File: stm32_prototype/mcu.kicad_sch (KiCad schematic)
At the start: 26 parts, among them SW1 BOOT0, SW2 RESET, U1 STM32F103C8T6, Y1 8MHz, Y2 32.768kHz

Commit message: Rev C schematic: STM32 RC-car controller
- New sheets power / drive / io replace power_usb / connectors
- 2S-3S battery on XT30 with AO4407A reverse protection, SMAJ15A, VBAT sense divider
- TPS563201 5 V / 3 A buck for servos and receiver; logic 5 V ORed from servo rail and USB
- DRV8870 brushed motor driver (3.3 A trip), 4 servo/ESC outputs, 3 receiver inputs,
  2 low-side light outputs, LSM6DS3TR-C IMU on I2C2, UART and 2x5 expansion header
- Project symbol library rcboard.kicad_sym (DRV8870, AO4407A)
- ERC 0/0, netlist matches all 74 intended nets (scripts/revc_schematic)

Co-Authored-By: Claude Opus 5.5 (1M context) <noreply@anthropic.com>
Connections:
- net PB10 is gone; now on net I2C_SCL: U1.21 (PB10)
- net PB11 is gone; now on net I2C_SDA: U1.22 (PB11)
- net I2C_SCL: no longer U1.42 (PB6)
- net I2C_SDA: no longer U1.43 (PB7)
- net PA0 renamed SERVO1
- net PA1 renamed SERVO2
- net PA10 renamed UART_RX
- net PA2 renamed SERVO3
- net PA3 renamed SERVO4
- net PA4 renamed VBAT_SENSE
- net PA6 renamed MOTOR_IN1
- net PA7 renamed MOTOR_IN2
- net PA9 renamed UART_TX
- net PB0 renamed LIGHT1
- net PB1 renamed LIGHT2
- net PB12 renamed IMU_INT1
- net PB13 renamed IMU_INT2
- net PB8 renamed RC_IN3
- net VBAT renamed VBAT_RTC
- new net RC_IN1: U1.42 (PB6)
- new net RC_IN2: U1.43 (PB7)
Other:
- note added: "Pin map: PA0-PA3 SERVO1-4 (TIM2 CH1-4) | PA4 VBAT_SENSE (ADC) | PA6/PA7 MOTOR_IN1/2 (TIM3 CH1/2) PB0/PB1 LIGHT1/2 (TIM3 CH3/4) | PB6-PB8 RC_IN1-3 (TIM4 CH1-3, 5 V tolerant) | PA9/PA10 USART1 PB10/PB11 I2C2 (IMU + Qwiic) | PB12/PB13 IMU INT1/INT2 | PC13 user LED (low-active) HSE 8 MHz, C_L = 12 pF: C = 2*(12 pF - 4 pF) = 16 pF -> 15 pF C0G. LSE optional (DNP)."
- note removed: "HSE: X32258MOB4SI 8 MHz, C_L = 12 pF. C1 = C2 = 2*(C_L - C_stray) = 2*(12 pF - 4 pF) = 16 pF -> 15 pF C0G. LSE (DNP): Q13FC13500049 32.768 kHz, C_L = 6 pF -> 2*(6 pF - 4 pF) = 4 pF -> 4.7 pF C0G. C_stray ~ 3-5 pF, verify on bring-up. USB: 0R series resistors (replace with 22R if needed). 1.5k D+ pull-up to 3V3 (F103 has no internal pull-up). VBAT tied to 3V3 via solder jumper (cut to run VBAT fro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"

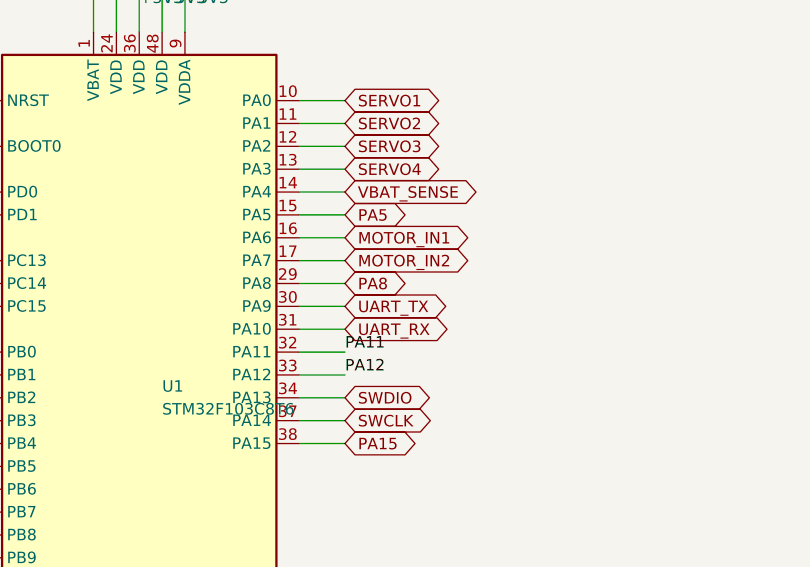
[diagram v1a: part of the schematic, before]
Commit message: Rev C: WS2812 RGB lighting output for 6 LEDs
- PA8 (TIM1 CH1 + DMA) -> SN74AHCT1G125 at 5 V -> 330R -> 3-pin connector (5V, DIN, GND),
  22 uF at the connector; PA8 removed from the expansion header
- Board re-placed and re-routed: DRC 0 violations, 0 unconnected, 0 parity issues; bottom silk 'RGB 5V DI G'
- Firmware: 800 kHz WS2812 driver via DMA, default head/sill/tail colours, 'c' colour and 'ind' indicator
  commands; builds (30 KB flash)
- Fabrication data, schematic images, renders and docs updated

Co-Authored-By: Claude Opus 5.5 (1M context) <noreply@anthropic.com>
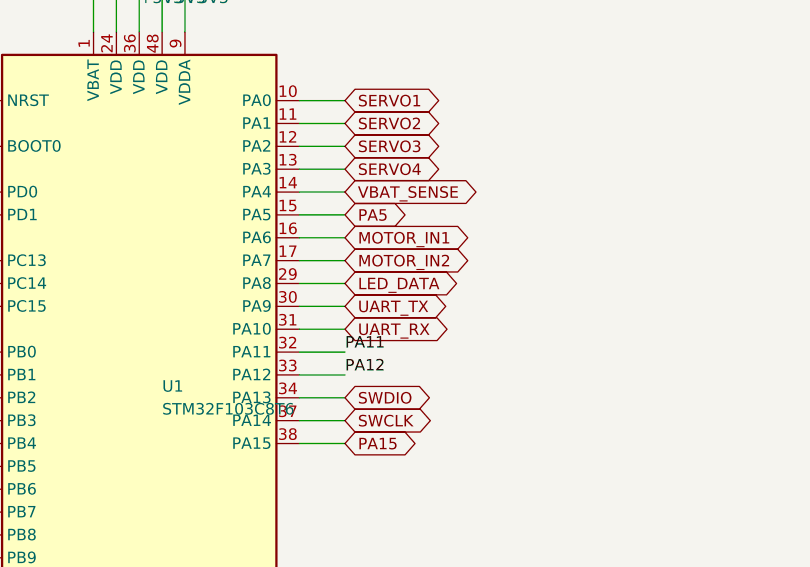
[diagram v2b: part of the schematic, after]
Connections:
- net PA8 renamed LED_DATA
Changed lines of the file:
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@@
 		)
 	)
-	(global_label "PA8"
+	(global_label "LED_DATA"
 		(shape bidirectional)
 		(at 226.06 134.62 0)
